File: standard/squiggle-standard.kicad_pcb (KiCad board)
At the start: 2 copper layers, 116 x 115.3 mm, 36 parts, among them SW1 switch, SW10 switch, SW11 switch, SW12 switch, SW13 switch, SW14 switch, SW15 switch, SW16 switch, SW17 switch, SW2 switch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

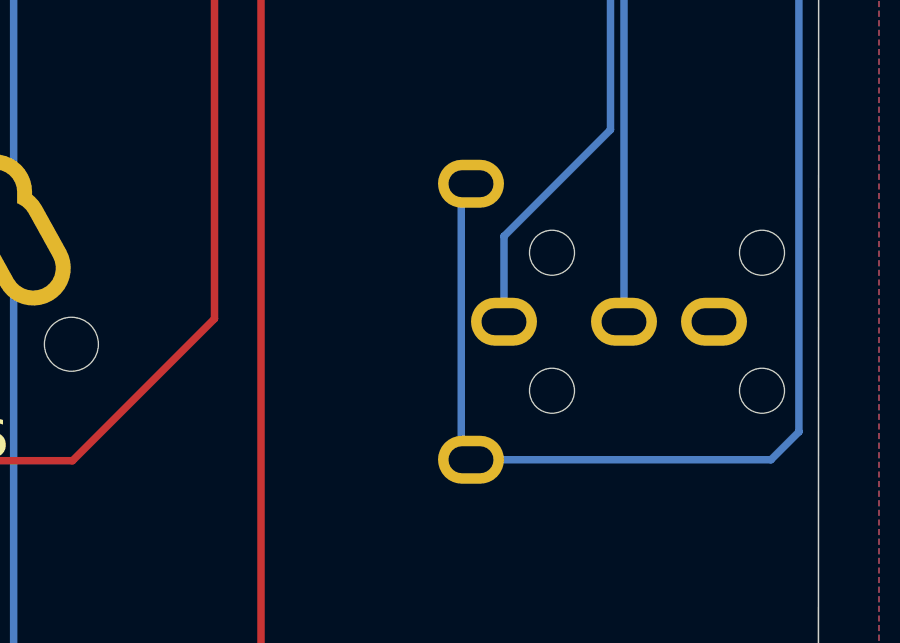
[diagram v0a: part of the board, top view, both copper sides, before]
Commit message: added stl files for the standard case.
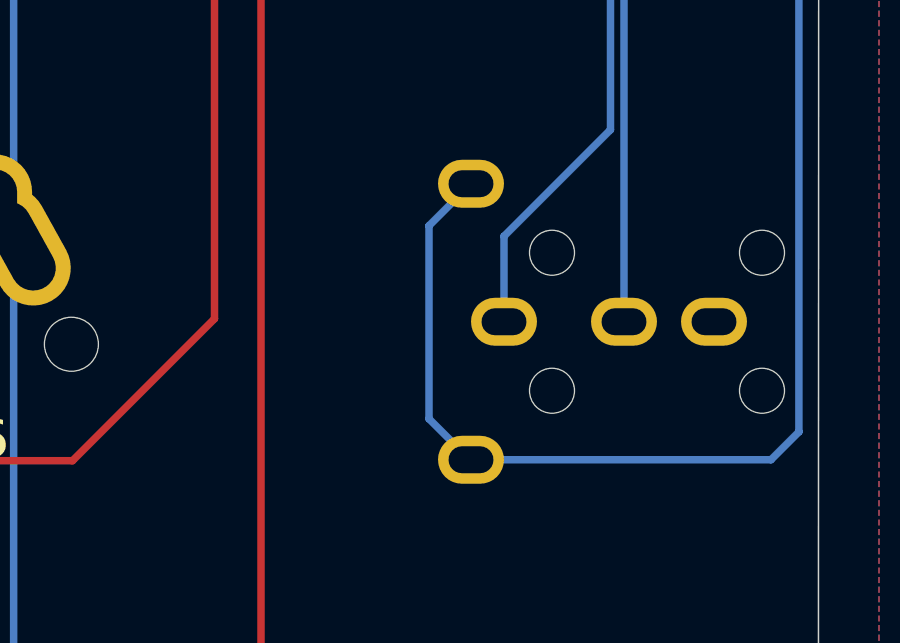
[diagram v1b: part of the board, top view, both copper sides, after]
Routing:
- net SDA: track 54.5 -> 55.4 mm
